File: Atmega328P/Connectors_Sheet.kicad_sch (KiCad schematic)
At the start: 4 parts, among them J1 Conn_01x04_Pin, J2 Conn_01x04_Pin, J3 Conn_01x09_Pin, J4 Conn_02x03_Odd_Even

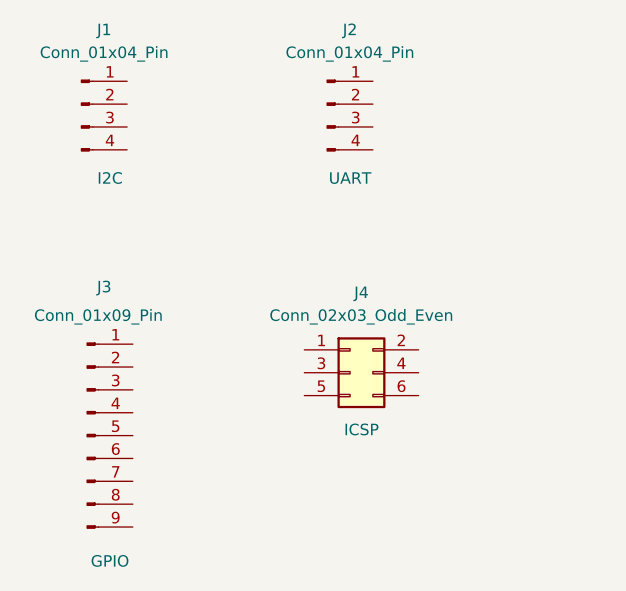
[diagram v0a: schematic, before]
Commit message: Componenets Value addded
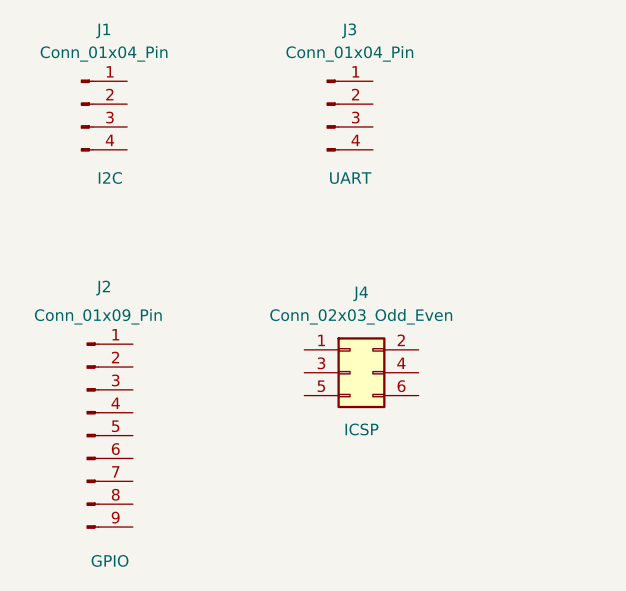
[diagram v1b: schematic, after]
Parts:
- renumbered J3 to J2, J2 to J3
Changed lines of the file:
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@@
 		(in_pos_files yes)
 		(dnp no)
-		(property "Reference" "J2"
+		(property "Reference" "J3"
 			(at 127.635 56.515 0)
 			(show_name no)
@@
 			(project "Atmega328P"
 				(path "/a3059dbd-d55d-42c4-a0da-e973b539ab98/468e35be-b99a-4502-8874-1fb5356543ab"
-					(reference "J2")
+					(reference "J3")
 					(unit 1)
 				)
@@
 		(in_pos_files yes)
 		(dnp no)
-		(property "Reference" "J3"
+		(property "Reference" "J2"
 			(at 100.33 85.09 0)
 			(show_name no)
@@
 			(project "Atmega328P"
 				(path "/a3059dbd-d55d-42c4-a0da-e973b539ab98/468e35be-b99a-4502-8874-1fb5356543ab"
-					(reference "J3")
+					(reference "J2")
 					(unit 1)
 				)

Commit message: Added the footprint for all symbols
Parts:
- J1, J3: footprint (none) -> Connector_PinHeader_2.54mm:PinHeader_1x04_P2.54mm_Vertical
- J2: footprint (none) -> Connector_PinHeader_2.54mm:PinHeader_1x09_P2.54mm_Vertical
- J4: footprint (none) -> Connector_PinHeader_2.54mm:PinHeader_2x03_P2.54mm_Vertical
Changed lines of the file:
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@@
 			)
 		)
-		(property "Footprint" ""
+		(property "Footprint" "Connector_PinHeader_2.54mm:PinHeader_1x04_P2.54mm_Vertical"
 			(at 97.79 64.77 0)
 			(hide yes)
@@
 			)
 		)
-		(property "Footprint" ""
+		(property "Footprint" "Connector_PinHeader_2.54mm:PinHeader_1x04_P2.54mm_Vertical"
 			(at 125.095 64.77 0)
 			(hide yes)
@@
 			)
 		)
-		(property "Footprint" ""
+		(property "Footprint" "Connector_PinHeader_2.54mm:PinHeader_1x09_P2.54mm_Vertical"
 			(at 98.425 101.6 0)
 			(hide yes)
@@
 			)
 		)
-		(property "Footprint" ""
+		(property "Footprint" "Connector_PinHeader_2.54mm:PinHeader_2x03_P2.54mm_Vertical"
 			(at 127.635 94.615 0)
 			(hide yes)

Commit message: Routing completed
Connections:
- net GND: now reaches J1.1 (Pin_1)
- net GND: now also J2.8 (Pin_8), J3.1 (Pin_1), J4.2 (Pin_2)
- net Vcc: now reaches J1.2 (Pin_2)
- net Vcc: now also J2.9 (Pin_9), J3.2 (Pin_2), J4.6 (Pin_6)
- net SDA: now reaches J1.3 (Pin_3)
- net SCL: now reaches J1.4 (Pin_4)
- net RX: now reaches J3.3 (Pin_3)
- net TX: now reaches J3.4 (Pin_4)
- net D2: now reaches J2.1 (Pin_1)
- net D3: now reaches J2.2 (Pin_2)
- net D4: now reaches J2.3 (Pin_3)
- net D5: now reaches J2.4 (Pin_4)
- net D6: now reaches J2.5 (Pin_5)
- net D7: now reaches J2.6 (Pin_6)
- net D8: now reaches J2.7 (Pin_7)
- net MOSI: now reaches J4.1 (Pin_1)
- net SCK: now reaches J4.3 (Pin_3)
- net MISO: now reaches J4.4 (Pin_4)
- net RESET: now reaches J4.5 (Pin_5)
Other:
- moved on the sheet: J3, J4

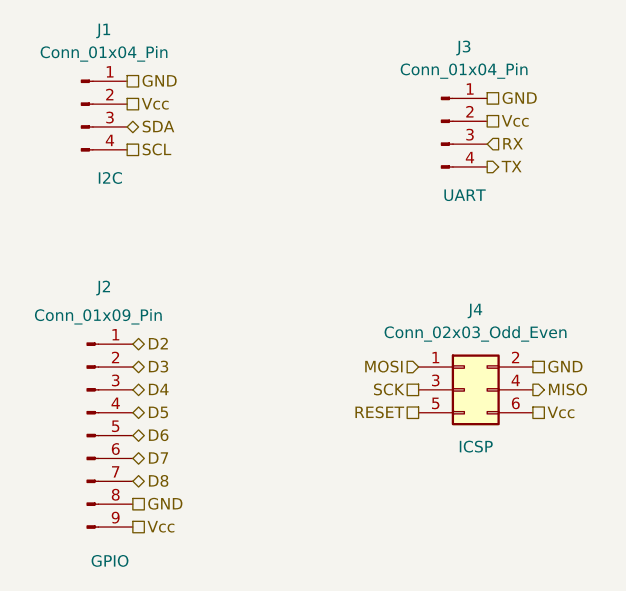
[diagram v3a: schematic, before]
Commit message: SCL Error - fixed
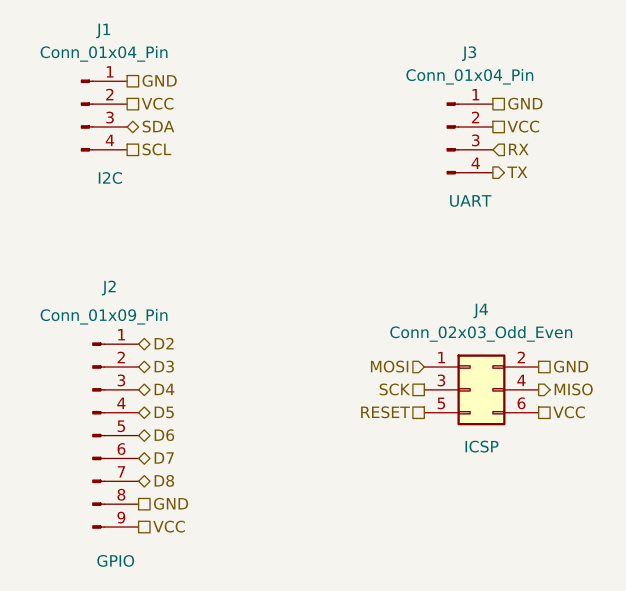
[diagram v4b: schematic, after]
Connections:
- net Vcc renamed VCC
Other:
- moved on the sheet: J2, J3, J4
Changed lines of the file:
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@@
 	(hierarchical_label "GND"
 		(shape passive)
-		(at 142.875 64.135 0)
+		(at 143.51 64.77 0)
 		(effects
 			(font
@@
 	(hierarchical_label "TX"
 		(shape output)
-		(at 142.875 71.755 0)
-		(effects
-			(font
-				(size 1.27 1.27)
-			)
-			(justify left)
-		)
-	)
-	(hierarchical_label "Vcc"
-		(shape passive)
-		(at 147.955 99.06 0)
+		(at 143.51 72.39 0)
+		(effects
+			(font
+				(size 1.27 1.27)
+			)
+			(justify left)
+		)
+	)
+	(hierarchical_label "VCC"
+		(shape passive)
+		(at 148.59 99.06 0)
 		(effects
 			(font
@@
 	(hierarchical_label "GND"
 		(shape passive)
-		(at 103.505 109.22 0)
+		(at 104.14 109.22 0)
 		(effects
 			(font
@@
 	(hierarchical_label "RX"
 		(shape input)
-		(at 142.875 69.215 0)
+		(at 143.51 69.85 0)
 		(effects
 			(font
@@
 	(hierarchical_label "D8"
 		(shape bidirectional)
-		(at 103.505 106.68 0)
+		(at 104.14 106.68 0)
 		(effects
 			(font
@@
 	(hierarchical_label "RESET"
 		(shape passive)
-		(at 135.255 99.06 180)
+		(at 135.89 99.06 180)
 		(effects
 			(font
@@
 	(hierarchical_label "MISO"
 		(shape output)
-		(at 147.955 96.52 0)
+		(at 148.59 96.52 0)
 		(effects
 			(font
@@
 	(hierarchical_label "D3"
 		(shape bidirectional)
-		(at 103.505 93.98 0)
+		(at 104.14 93.98 0)
 		(effects
 			(font
@@
 	(hierarchical_label "GND"
 		(shape passive)
-		(at 147.955 93.98 0)
+		(at 148.59 93.98 0)
 		(effects
 			(font
@@
 	(hierarchical_label "D2"
 		(shape bidirectional)
-		(at 103.505 91.44 0)
+		(at 104.14 91.44 0)
 		(effects
 			(font
@@
 	(hierarchical_label "D4"
 		(shape bidirectional)
-		(at 103.505 96.52 0)
+		(at 104.14 96.52 0)
 		(effects
 			(font
@@
 	(hierarchical_label "D7"
 		(shape bidirectional)
-		(at 103.505 104.14 0)
+		(at 104.14 104.14 0)
 		(effects
 			(font
@@
 	(hierarchical_label "D6"
 		(shape bidirectional)
-		(at 103.505 101.6 0)
+		(at 104.14 101.6 0)
 		(effects
 			(font
@@
 	(hierarchical_label "D5"
 		(shape bidirectional)
-		(at 103.505 99.06 0)
-		(effects
-			(font
-				(size 1.27 1.27)
-			)
-			(justify left)
-		)
-	)
-	(hierarchical_label "Vcc"
-		(shape passive)
-		(at 142.875 66.675 0)
+		(at 104.14 99.06 0)
+		(effects
+			(font
+				(size 1.27 1.27)
+			)
+			(justify left)
+		)
+	)
+	(hierarchical_label "VCC"
+		(shape passive)
+		(at 143.51 67.31 0)
 		(effects
 			(font
@@
 	(hierarchical_label "SCK"
 		(shape passive)
-		(at 135.255 96.52 180)
+		(at 135.89 96.52 180)
 		(effects
 			(font
@@
 		)
 	)
-	(hierarchical_label "Vcc"
-		(shape passive)
-		(at 103.505 111.76 0)
+	(hierarchical_label "VCC"
+		(shape passive)
+		(at 104.14 111.76 0)
 		(effects
 			(font
@@
 	(hierarchical_label "MOSI"
 		(shape input)
-		(at 135.255 93.98 180)
+		(at 135.89 93.98 180)
 		(effects
 			(font
@@
 		)
 	)
-	(hierarchical_label "Vcc"
+	(hierarchical_label "VCC"
 		(shape passive)
 		(at 102.87 64.77 0)
@@
 	(symbol
 		(lib_id "Connector:Conn_01x04_Pin")
-		(at 137.795 66.675 0)
+		(at 138.43 67.31 0)
 		(unit 1)
 		(body_style 1)
@@
 		(dnp no)
 		(property "Reference" "J3"
-			(at 140.335 58.42 0)
+			(at 140.97 59.055 0)
 			(show_name no)
 			(do_not_autoplace no)
@@
 		)
 		(property "Value" "Conn_01x04_Pin"
-			(at 140.335 60.96 0)
+			(at 140.97 61.595 0)
 			(show_name no)
 			(do_not_autoplace no)
@@
 		)
 		(property "Footprint" "Connector_PinHeader_2.54mm:PinHeader_1x04_P2.54mm_Vertical"
-			(at 137.795 66.675 0)
+			(at 138.43 67.31 0)
 			(hide yes)
 			(show_name no)
@@
 		)
 		(property "Datasheet" ""
-			(at 137.795 66.675 0)
+			(at 138.43 67.31 0)
 			(hide yes)
 			(show_name no)
@@
 		)
 		(property "Description" "Generic connector, single row, 01x04, script generated"
-			(at 137.795 66.675 0)
+			(at 138.43 67.31 0)
 			(hide yes)
 			(show_name no)
@@
 		)
 		(property "Name" "UART"
-			(at 140.335 74.93 0)
+			(at 140.97 75.565 0)
 			(show_name no)
 			(do_not_autoplace no)
@@
 	(symbol
 		(lib_id "Connector:Conn_01x09_Pin")
-		(at 98.425 101.6 0)
+		(at 99.06 101.6 0)
 		(unit 1)
 		(body_style 1)
@@
 		(dnp no)
 		(property "Reference" "J2"
-			(at 100.33 85.09 0)
+			(at 100.965 85.09 0)
 			(show_name no)
 			(do_not_autoplace no)
@@
 		)
 		(property "Value" "Conn_01x09_Pin"
-			(at 99.695 88.265 0)
+			(at 100.33 88.265 0)
 			(show_name no)
 			(do_not_autoplace no)
@@
 		)
 		(property "Footprint" "Connector_PinHeader_2.54mm:PinHeader_1x09_P2.54mm_Vertical"
-			(at 98.425 101.6 0)
+			(at 99.06 101.6 0)
 			(hide yes)
 			(show_name no)
@@
 		)
 		(property "Datasheet" ""
-			(at 98.425 101.6 0)
+			(at 99.06 101.6 0)
 			(hide yes)
 			(show_name no)
@@
 		)
 		(property "Description" "Generic connector, single row, 01x09, script generated"
-			(at 98.425 101.6 0)
+			(at 99.06 101.6 0)
 			(hide yes)
 			(show_name no)
@@
 		)
 		(property "Name" "GPIO"
-			(at 100.965 115.57 0)
+			(at 101.6 115.57 0)
 			(show_name no)
 			(do_not_autoplace no)
@@
 	(symbol
 		(lib_id "Connector_Generic:Conn_02x03_Odd_Even")
-		(at 140.335 96.52 0)
+		(at 140.97 96.52 0)
 		(unit 1)
 		(body_style 1)
@@
 		(dnp no)
 		(property "Reference" "J4"
-			(at 141.605 87.63 0)
+			(at 142.24 87.63 0)
 			(show_name no)
 			(do_not_autoplace no)
@@
 		)
 		(property "Value" "Conn_02x03_Odd_Even"
-			(at 141.605 90.17 0)
+			(at 142.24 90.17 0)
 			(show_name no)
 			(do_not_autoplace no)
@@
 		)
 		(property "Footprint" "Connector_PinHeader_2.54mm:PinHeader_2x03_P2.54mm_Vertical"
-			(at 140.335 96.52 0)
+			(at 140.97 96.52 0)
 			(hide yes)
 			(show_name no)
@@
 		)
 		(property "Datasheet" ""
-			(at 140.335 96.52 0)
+			(at 140.97 96.52 0)
 			(hide yes)
 			(show_name no)
@@
 		)
 		(property "Description" "Generic connector, double row, 02x03, odd/even pin numbering scheme (row 1 odd numbers, row 2 even numbers), script generated (kicad-library-utils/schlib/autogen/connector/)"
-			(at 140.335 96.52 0)
+			(at 140.97 96.52 0)
 			(hide yes)
 			(show_name no)
@@
 		)
 		(property "Name" "ICSP"
-			(at 141.605 102.87 0)
-			(show_name no)
-			(do_not_autoplace no)
+			(at 142.24 102.87 0)
+			(show_name no)
+			(do_not_autoplace no)
